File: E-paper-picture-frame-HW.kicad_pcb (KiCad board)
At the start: 4 copper layers, 170.2 x 111.2 mm, 117 parts, among them J1 Connector, USB-TYPE-C-16P, J2 Conn_01x02, J3 Conn_01x02, Q1 AO3401A, Q2 BSS138, Q3 AO3400A, Q4 AO3401A, Q5 AO3401A, SW1 SK12D07VG4, U1 TPS63001DRCR, U2 TP4054, U3 ESP32-C6-MINI-1

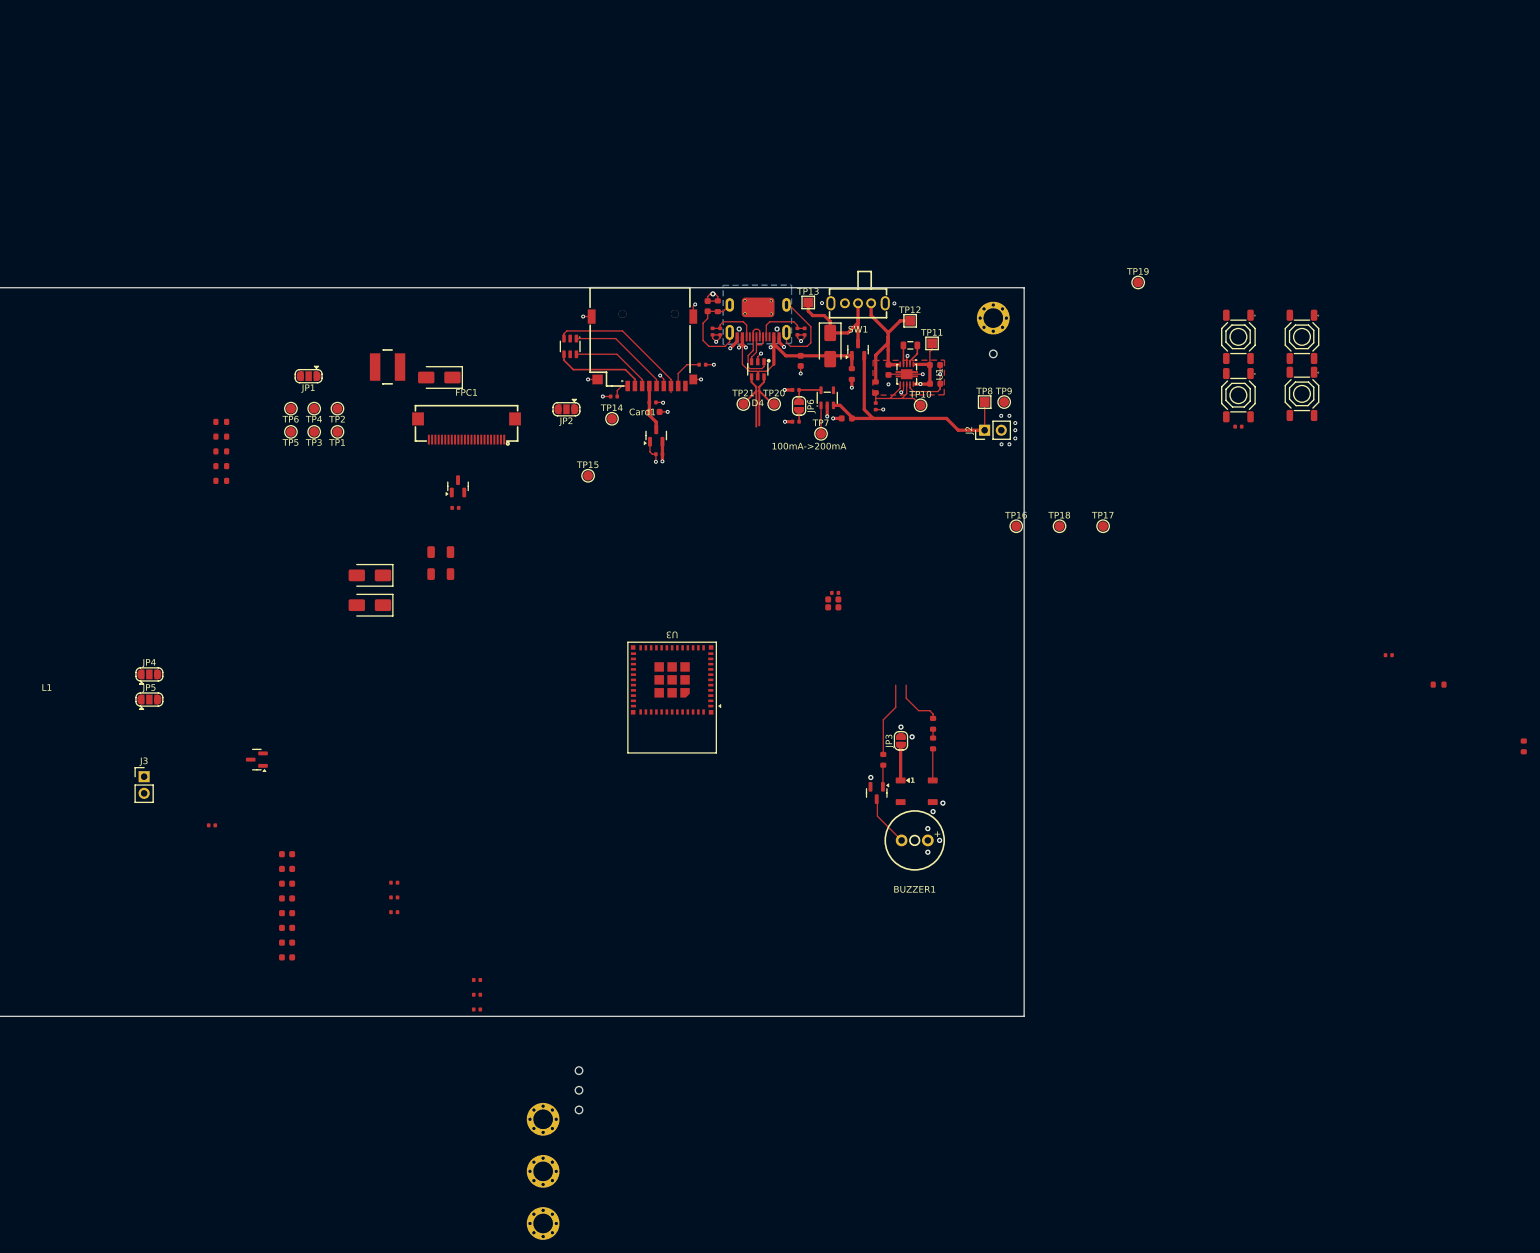
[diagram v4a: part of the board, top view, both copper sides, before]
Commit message: First draft of layout done. Needs cleaning and DRC
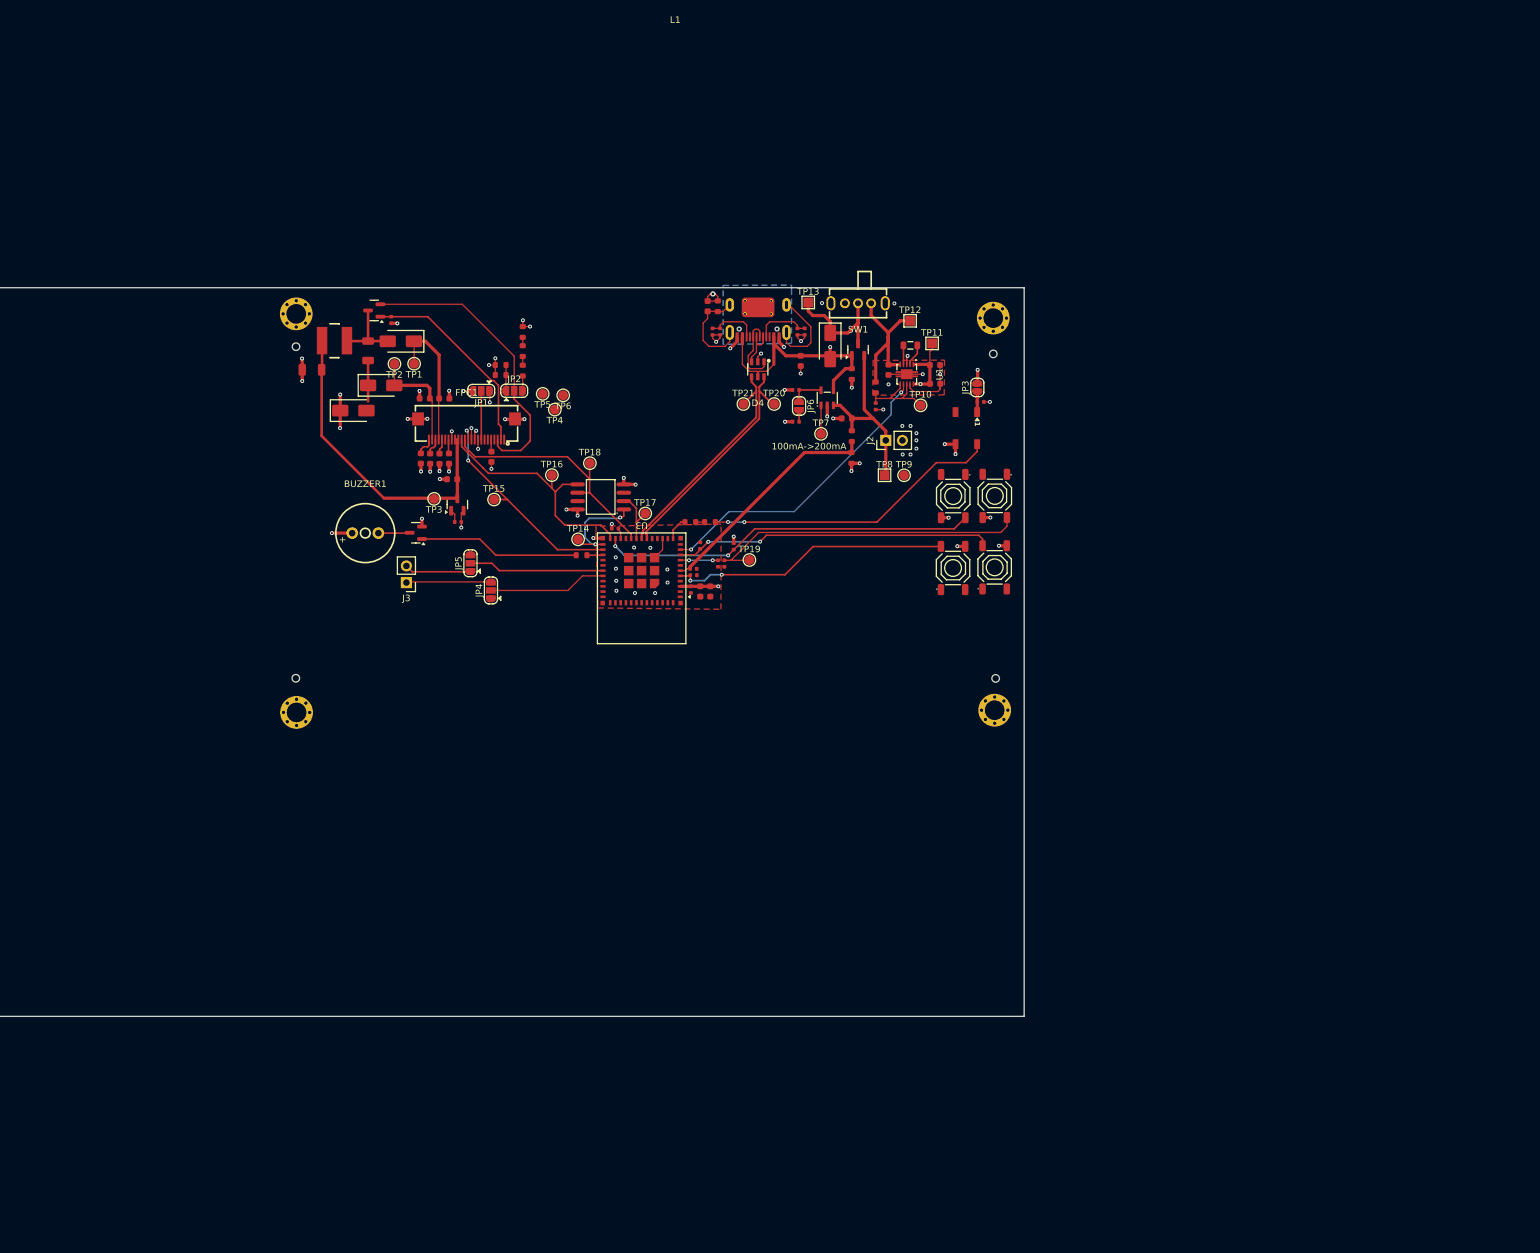
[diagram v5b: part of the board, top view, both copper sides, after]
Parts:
- removed C21: 10uF, PCM_JLCPCB:C_0603
- removed C22: 100nF, PCM_JLCPCB:C_0402
- removed Card1: TF PUSH, Libraries:TF-SMD_TF-PUSH
- removed D7: SRV05-4_C7420376, PCM_JLCPCB:SOT-23-6_L2.9-W1.6-P0.95-LS2.8-BL-1
- removed Q5: AO3401A, PCM_JLCPCB:Q_SOT-23
- removed R21, R22, R23: 10kΩ, PCM_JLCPCB:R_0402
- added U4: W25Q128, PCM_JLCPCB:SOIC-8_L5.3-W5.3-P1.27-LS8.0-BL, F.Cu at (128.5, 51.4)
- moved H2 128.6 mm to (82.0, 23.5)
- moved H8 124.2 mm to (82.0, 28.5)
- moved C13 117.2 mm to (186.4, 36.9)
- moved R17 113.0 mm to (166.8, 42.1), turned to -90 degrees
- moved C16 106.9 mm to (142.6, 62.4)
- moved H4 104.3 mm to (188.6, 84.0)
- moved BUZZER1 96.1 mm to (92.5, 57.0), turned to 0 degrees
- moved R18 96.0 mm to (166.8, 45.5), turned to -90 degrees
- moved H6 87.3 mm to (188.8, 79.1)
- moved C1 82.5 mm to (111.8, 45.3), turned to 90 degrees
- moved C23 82.1 mm to (146.4, 61.6), turned to -90 degrees
- moved R2 81.8 mm to (96.5, 24.4), turned to -90 degrees
- moved Q3 80.8 mm to (100.3, 56.9), turned to 180 degrees
- moved C6 80.0 mm to (104.6, 36.4), turned to 0 degrees
- moved H3 79.5 mm to (82.1, 84.3)
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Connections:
- net /MCU/SPI2.MISO renamed /Display/SPI.MISO
- C13 pad 2: /IO/LED_VDD -> GNDD
- U3 pad 12: /MCU/GPIO0 -> /IO/LED_DIN
- U3 pad 24: /MCU/GPIO18 -> /Display/SPI.MOSI
- U3 pad 29: /IO/LED_DIN -> /MCU/GPIO23
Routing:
- net /MCU/Boot: track 0.00 -> 57.6 mm, vias 0 -> 2
- net /MCU/EN: track 0.00 -> 55.1 mm, vias 0 -> 2
- net /IO/USER0: track 0.00 -> 48.6 mm, vias 0 -> 2
- net /Display/EPD3V3: track 0.00 -> 48.2 mm
- net /IO/PS/SYNC: track 1.41 -> 46.2 mm, vias 1 -> 2
- net /Display/RESE: track 0.00 -> 44.5 mm
- net GNDD: track 52.7 -> 95.6 mm, vias 34 -> 72
- net /IO/USER1: track 0.00 -> 42.8 mm, vias 0 -> 2
- net /IO/DIN: track 4.92 -> 45.8 mm, vias 0 -> 2
- net /IO/VBAT_MON: track 0.00 -> 35.5 mm
- net /Display/EPD CS: track 0.00 -> 34.4 mm, vias 0 -> 2
- net /IO/5V_USB: track 32.3 -> 63.4 mm, vias 3 -> 2
- net /Display/GDR: track 0.00 -> 30.8 mm
- net /Display/SPI.MOSI: track 12.6 -> 37.9 mm
- net /MCU/USB D+: track 10.5 -> 35.0 mm
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- added copper zone on In2.Cu, net +3.3V
